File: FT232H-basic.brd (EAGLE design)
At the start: 45.7 x 17.8 mm, 29 parts, among them IC1 FT232H

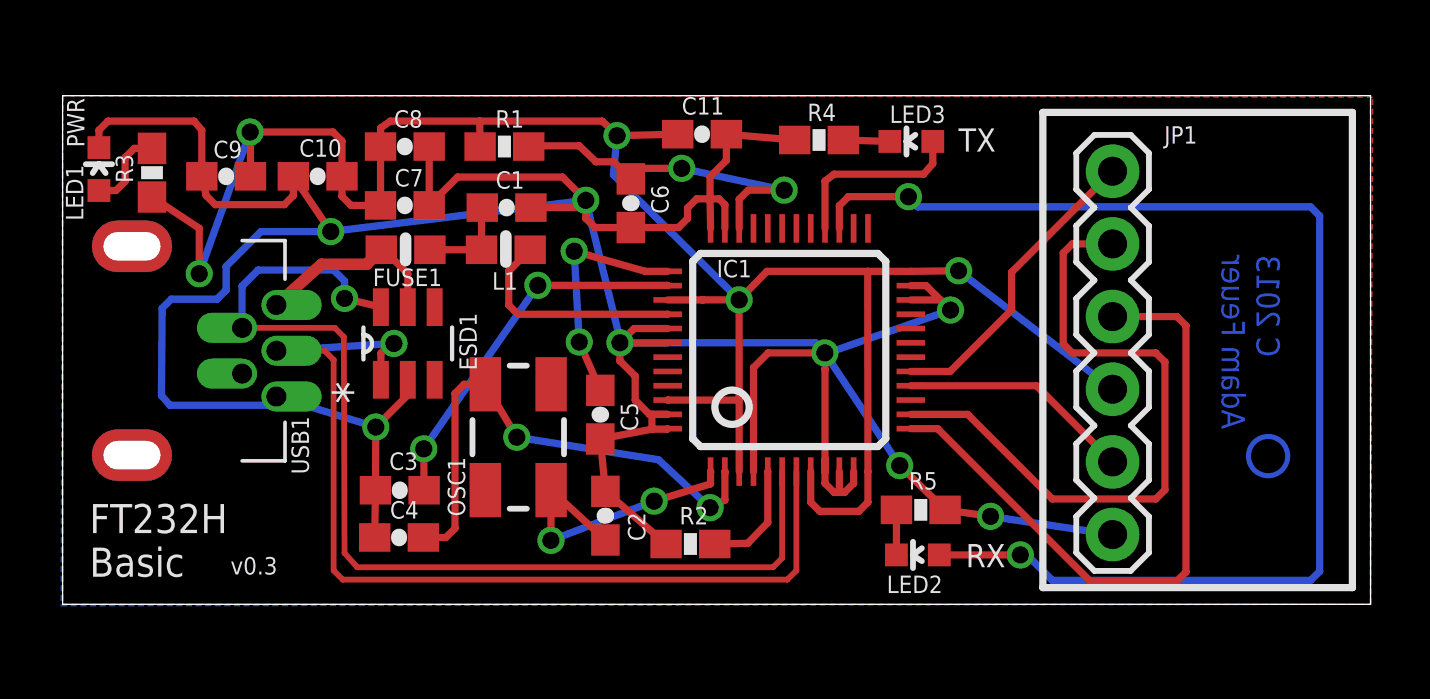
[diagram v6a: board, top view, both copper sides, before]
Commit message: rerouted board to make USB DM and DP signals as short as possible; USART data signals are on top of board; board is slightly wider; version bumped to 0.4
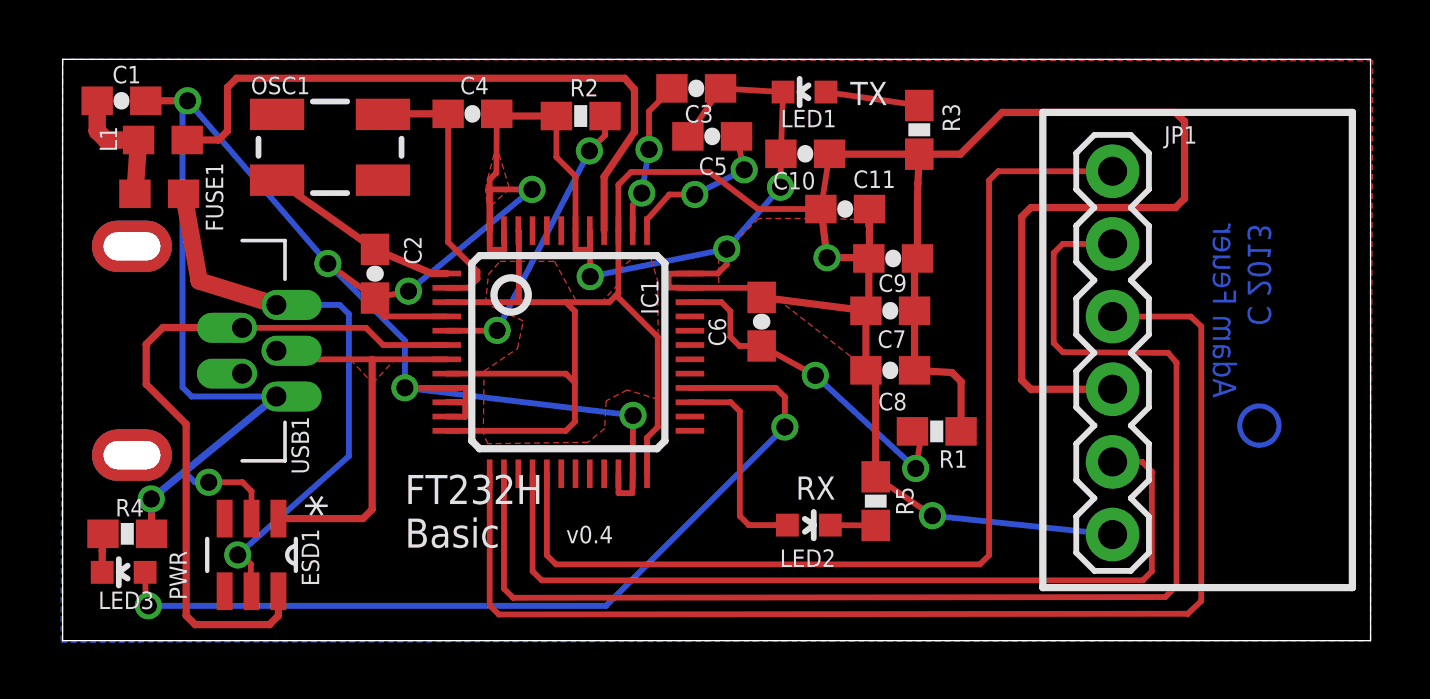
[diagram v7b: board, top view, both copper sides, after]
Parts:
- moved LED3 31.4 mm to (8.48, 6.20)
- moved R4 27.8 mm to (8.61, 7.54), turned to 180 degrees
- moved R3 26.9 mm to (36.3, 21.7)
- moved LED1 24.8 mm to (32.3, 23.0), turned to 90 degrees
- moved C9 23.5 mm to (35.4, 17.2)
- moved C8 18.7 mm to (35.3, 13.3), turned to 180 degrees
- moved R1 18.1 mm to (36.9, 11.1), turned to 0 degrees
- moved C3 17.5 mm to (28.5, 23.1), turned to 0 degrees
- moved C7 17.4 mm to (35.3, 15.3), turned to 180 degrees
- moved C10 17.1 mm to (32.3, 20.8)
- moved R2 15.4 mm to (24.5, 22.1)
- moved C4 15.0 mm to (20.7, 22.2), turned to 0 degrees
- moved C1 14.0 mm to (8.41, 22.7)
- moved L1 12.6 mm to (9.86, 21.3)
- moved OSC1 12.1 mm to (15.7, 21.1), turned to 0 degrees
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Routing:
- net RXLED: track 44.2 -> 7.33 mm, vias 2 -> 0
- net DTR: track 10.7 -> 36.1 mm
- net TXLED: track 6.45 -> 30.5 mm, vias 0 -> 2
- net CTS: track 8.16 -> 30.3 mm
- net RXI: track 23.6 -> 45.5 mm
- net DP: track 35.0 -> 14.7 mm, vias 1 -> 0
- net TXO: track 23.3 -> 42.6 mm
- net VREGIN: track 7.94 -> 22.9 mm
- net VUSB: track 6.86 -> 20.3 mm, vias 0 -> 1
- net DM: track 37.3 -> 25.4 mm, vias 1 -> 0
- net N$7: track 18.4 -> 9.68 mm, vias 2 -> 0
- net POWER: track 76.3 -> 84.5 mm, vias 5 -> 0
- net N$2: track 13.0 -> 5.43 mm
- net N$4: track 3.94 -> 10.3 mm, vias 0 -> 2
- net OSC1: track 10.7 -> 6.87 mm, vias 2 -> 0
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- added copper zone on layer 1, net DP
- added copper zone on layer 1, net GND
- added copper zone on layer 1, net POWER
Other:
- board size 45.7 x 17.8 mm -> 45.7 x 20.3 mm
- board text added: "v0.4"
- board text removed: "v0.3"

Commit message: fixed error with TX LED being in wrong place - power LED is now in lower left, TX in upper right-middle
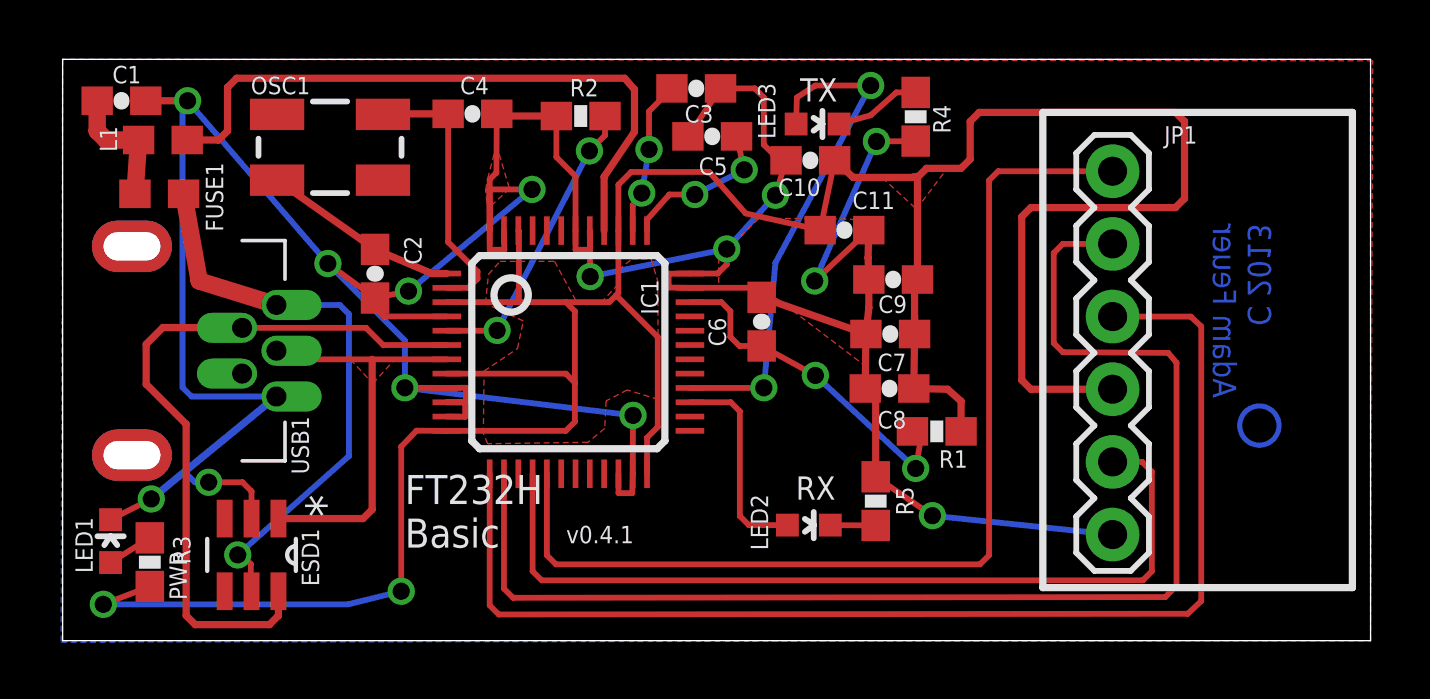
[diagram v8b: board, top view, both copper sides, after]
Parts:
- moved R4 31.2 mm to (36.2, 22.1), turned to 90 degrees
- moved R3 30.9 mm to (9.40, 6.55)
- moved LED1 28.9 mm to (8.03, 7.29), turned to 0 degrees
- moved LED3 28.9 mm to (32.7, 21.9), turned to 270 degrees
- moved C7 0.81 mm to (35.3, 14.5)
- moved C11 0.74 mm to (33.7, 18.2)
- moved C9 0.74 mm to (35.4, 16.4)
- moved C8 0.64 mm to (35.3, 12.6)
- moved C10 0.29 mm to (32.5, 20.6)
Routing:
- net POWER: track 84.5 -> 105.4 mm, vias 0 -> 2
- net TXLED: track 30.5 -> 17.6 mm
- net GND: track 133.2 -> 138.7 mm, vias 13 -> 14
- net N$10: track 1.35 -> 3.02 mm
- net N$5: track 3.30 -> 1.62 mm
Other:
- board text added: "v0.4.1"
- board text removed: "v0.4"
